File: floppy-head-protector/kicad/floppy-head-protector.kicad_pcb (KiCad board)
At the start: 2 copper layers, 133 x 180 mm, 0 parts

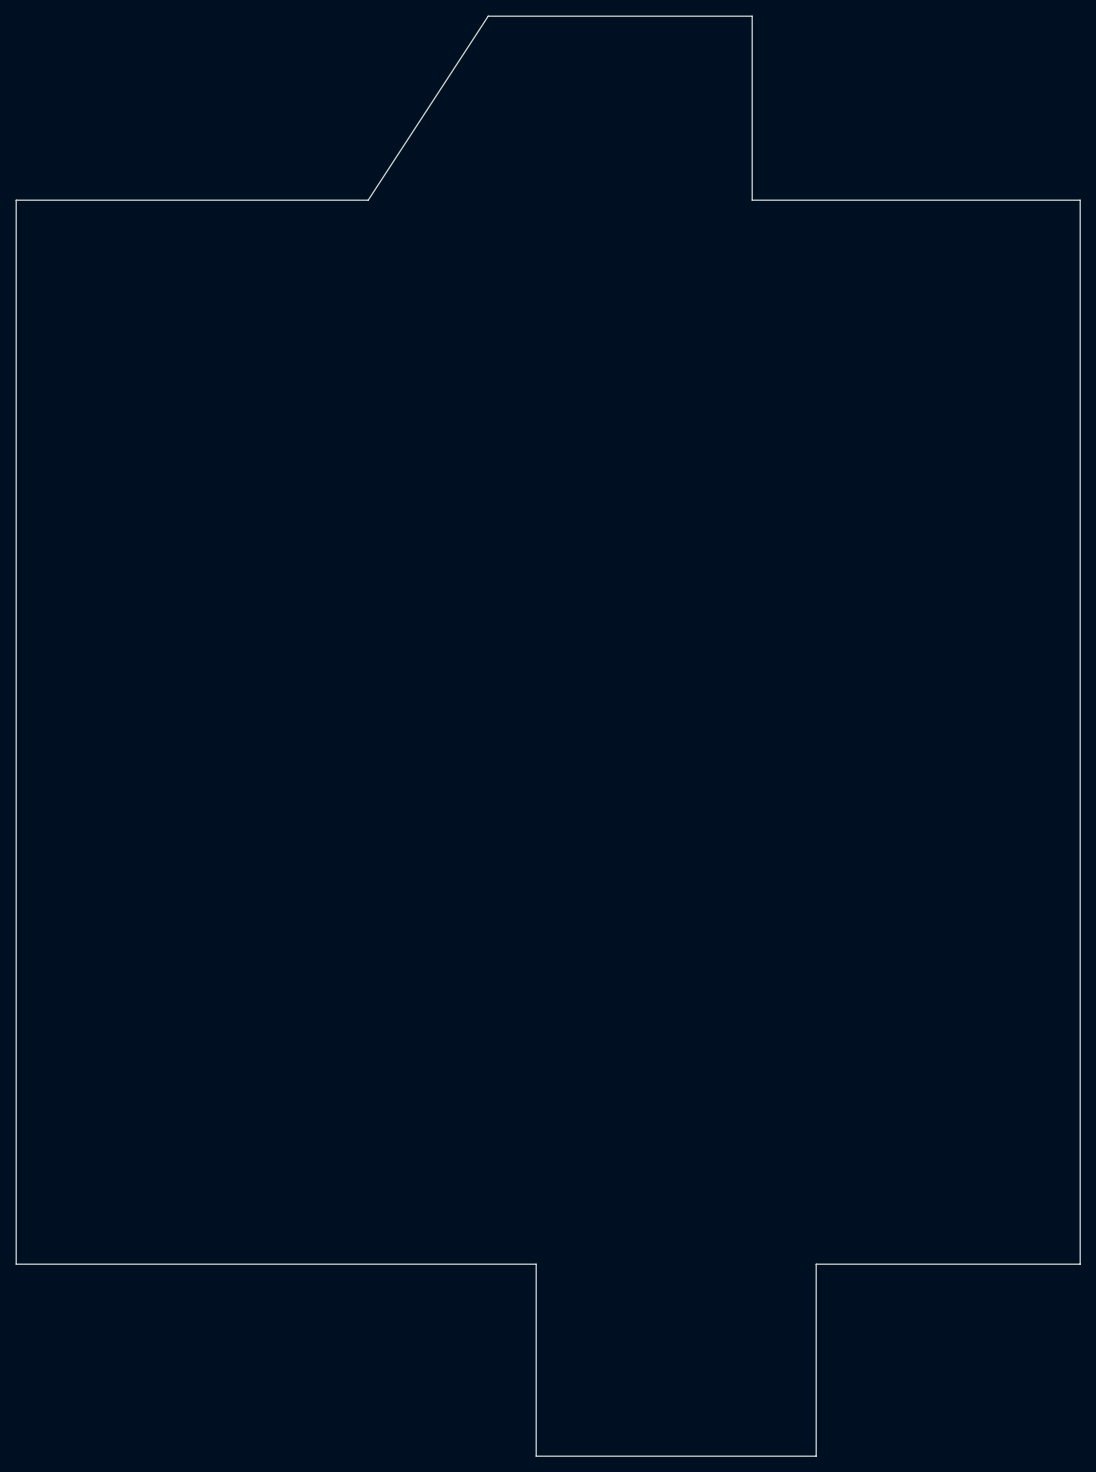
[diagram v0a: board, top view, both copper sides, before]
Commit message: WIP FHP: Shorten Y 3mm
- It was 1mm too large
- Remove 2 more mm because knife will cut a bit away from edge
- Still need to do this for Y
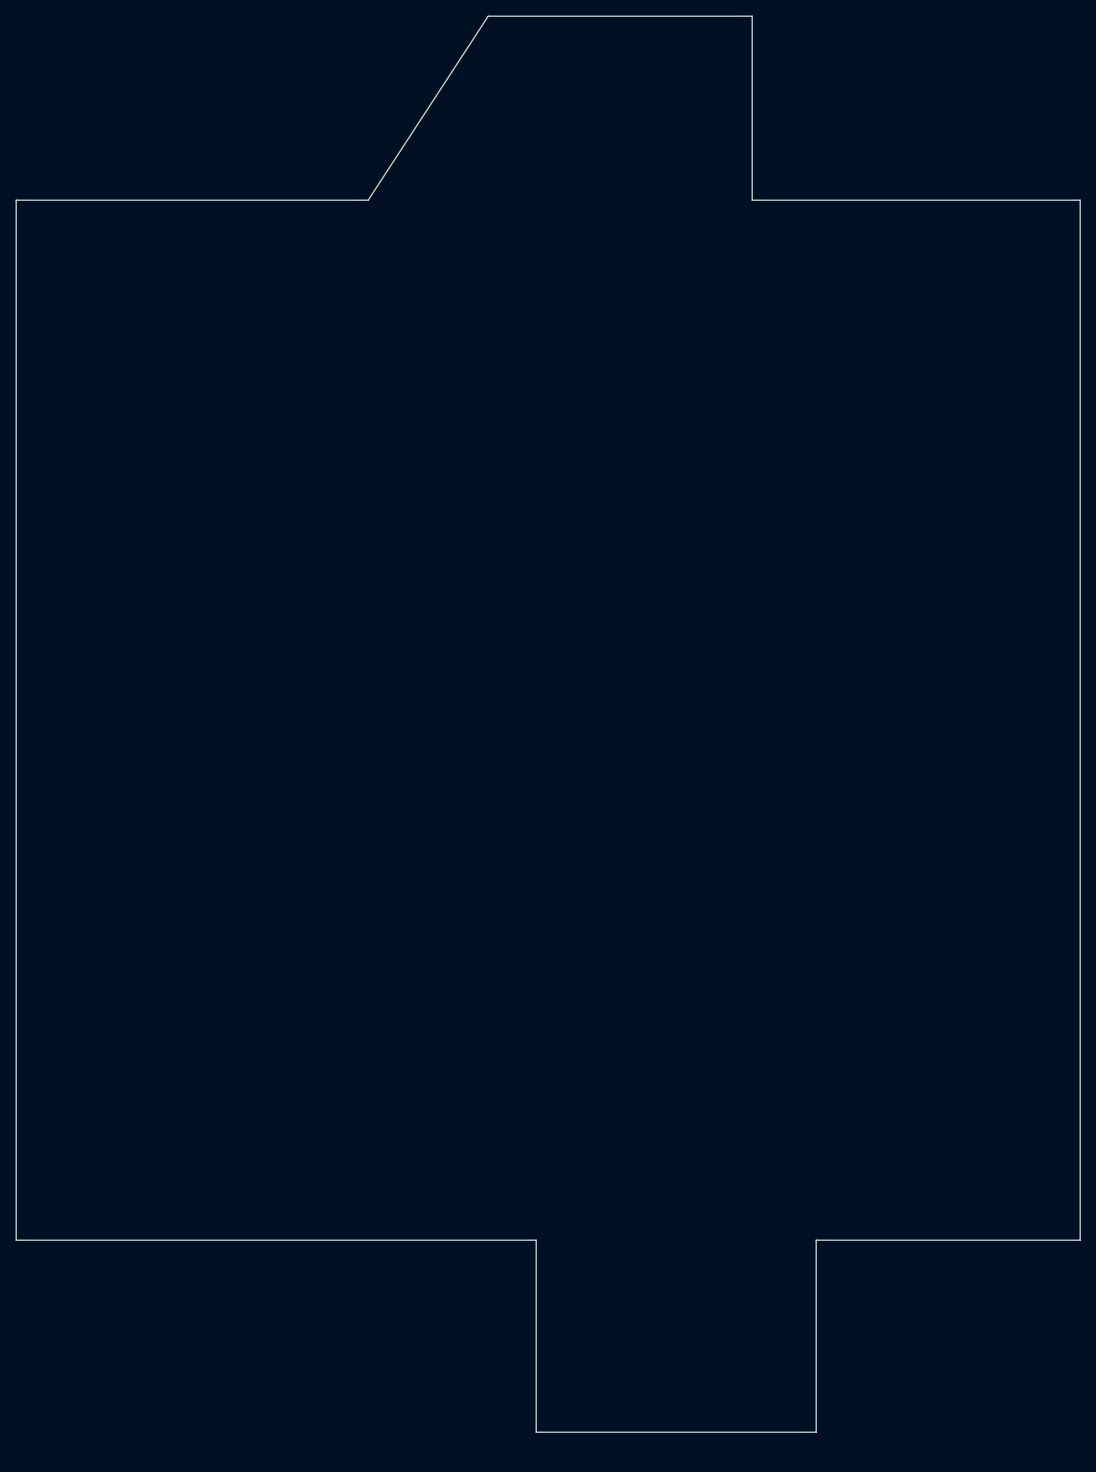
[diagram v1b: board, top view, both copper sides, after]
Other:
- board size 133 x 180 mm -> 133 x 177 mm
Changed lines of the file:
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@@
 	(net 0 "")
 	(gr_line
-		(start 95 187)
-		(end 130 187)
+		(start 95 184)
+		(end 130 184)
 		(stroke
 			(width 0.05)
@@
 	)
 	(gr_line
-		(start 95 163)
-		(end 95 187)
+		(start 95 160)
+		(end 95 184)
 		(stroke
 			(width 0.05)
@@
 	)
 	(gr_line
-		(start 130 163)
-		(end 130 187)
+		(start 130 160)
+		(end 130 184)
 		(stroke
 			(width 0.05)
@@
 	(gr_line
 		(start 30 30)
-		(end 30 163)
+		(end 30 160)
 		(stroke
 			(width 0.05)
@@
 	)
 	(gr_line
-		(start 30 163)
-		(end 95 163)
+		(start 30 160)
+		(end 95 160)
 		(stroke
 			(width 0.05)
@@
 	)
 	(gr_line
-		(start 130 163)
-		(end 163 163)
+		(start 130 160)
+		(end 163 160)
 		(stroke
 			(width 0.05)
@@
 	(gr_line
 		(start 163 30)
-		(end 163 163)
+		(end 163 160)
 		(stroke
 			(width 0.05)
